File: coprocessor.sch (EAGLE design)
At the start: 51 parts, among them IC1 MEGA32U2, J1 AVR_SPI_PRG_6NS, U1 TPS61090RSAR, U3 V_REG_LDOSMD2, U4 AZV321

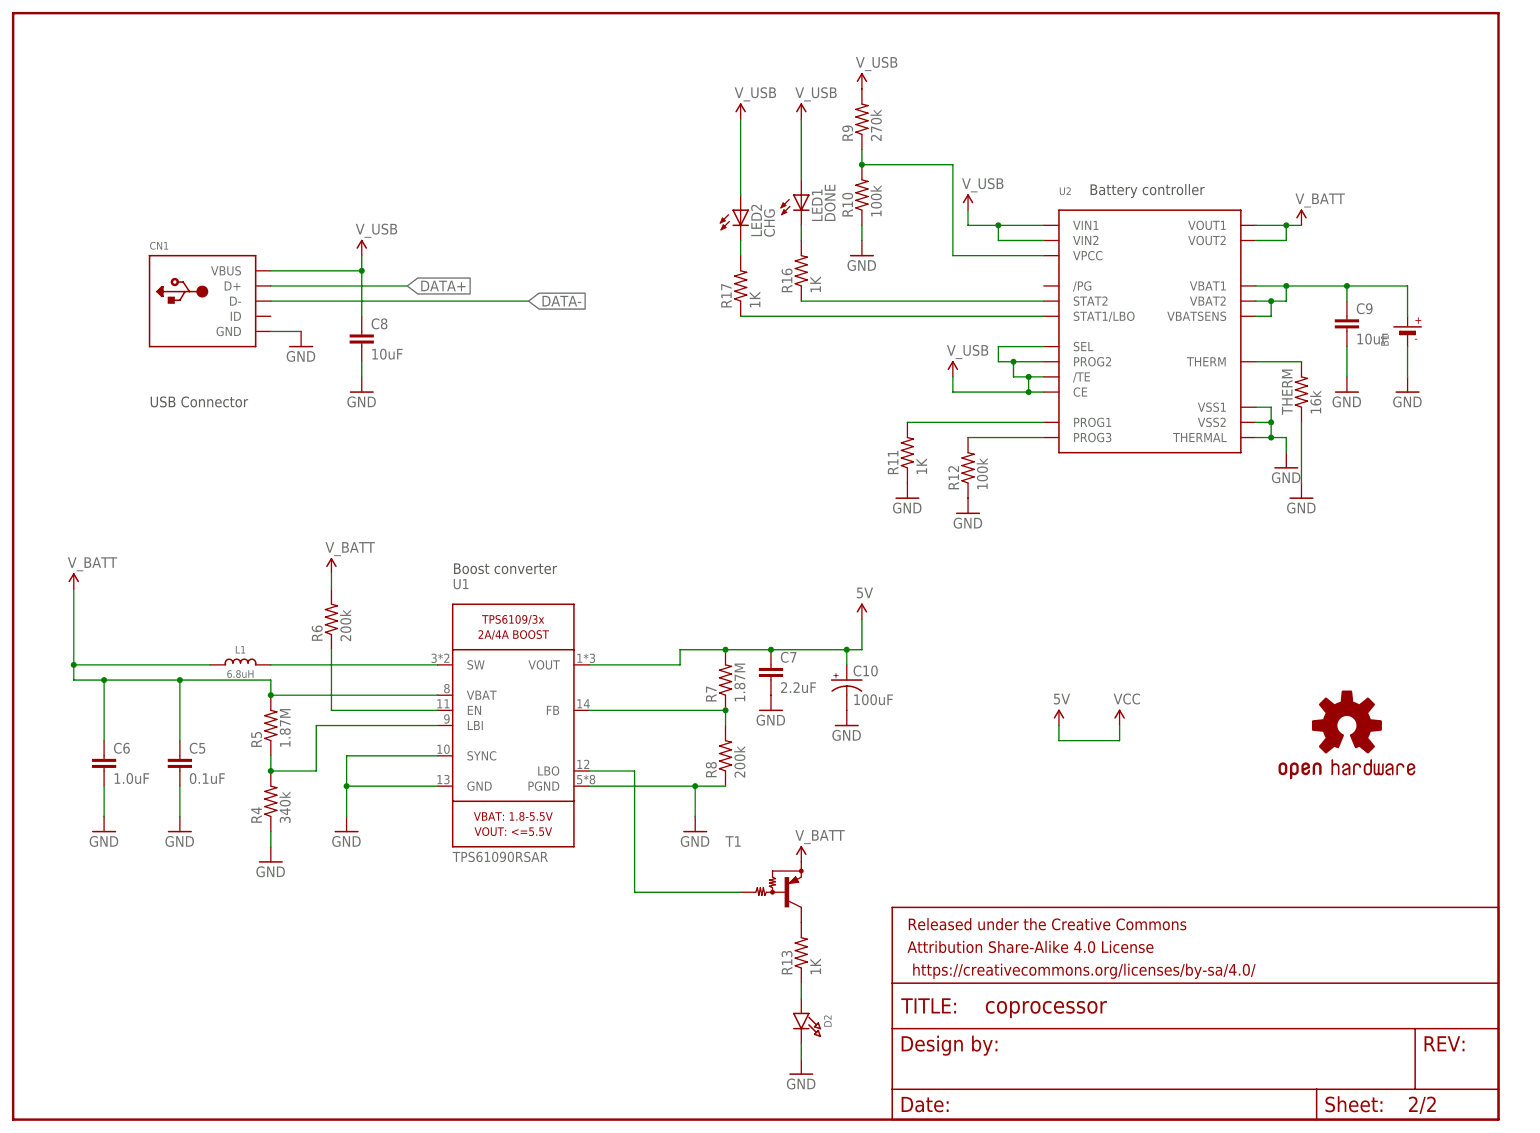
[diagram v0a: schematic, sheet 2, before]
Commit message: final schematic for revision 2
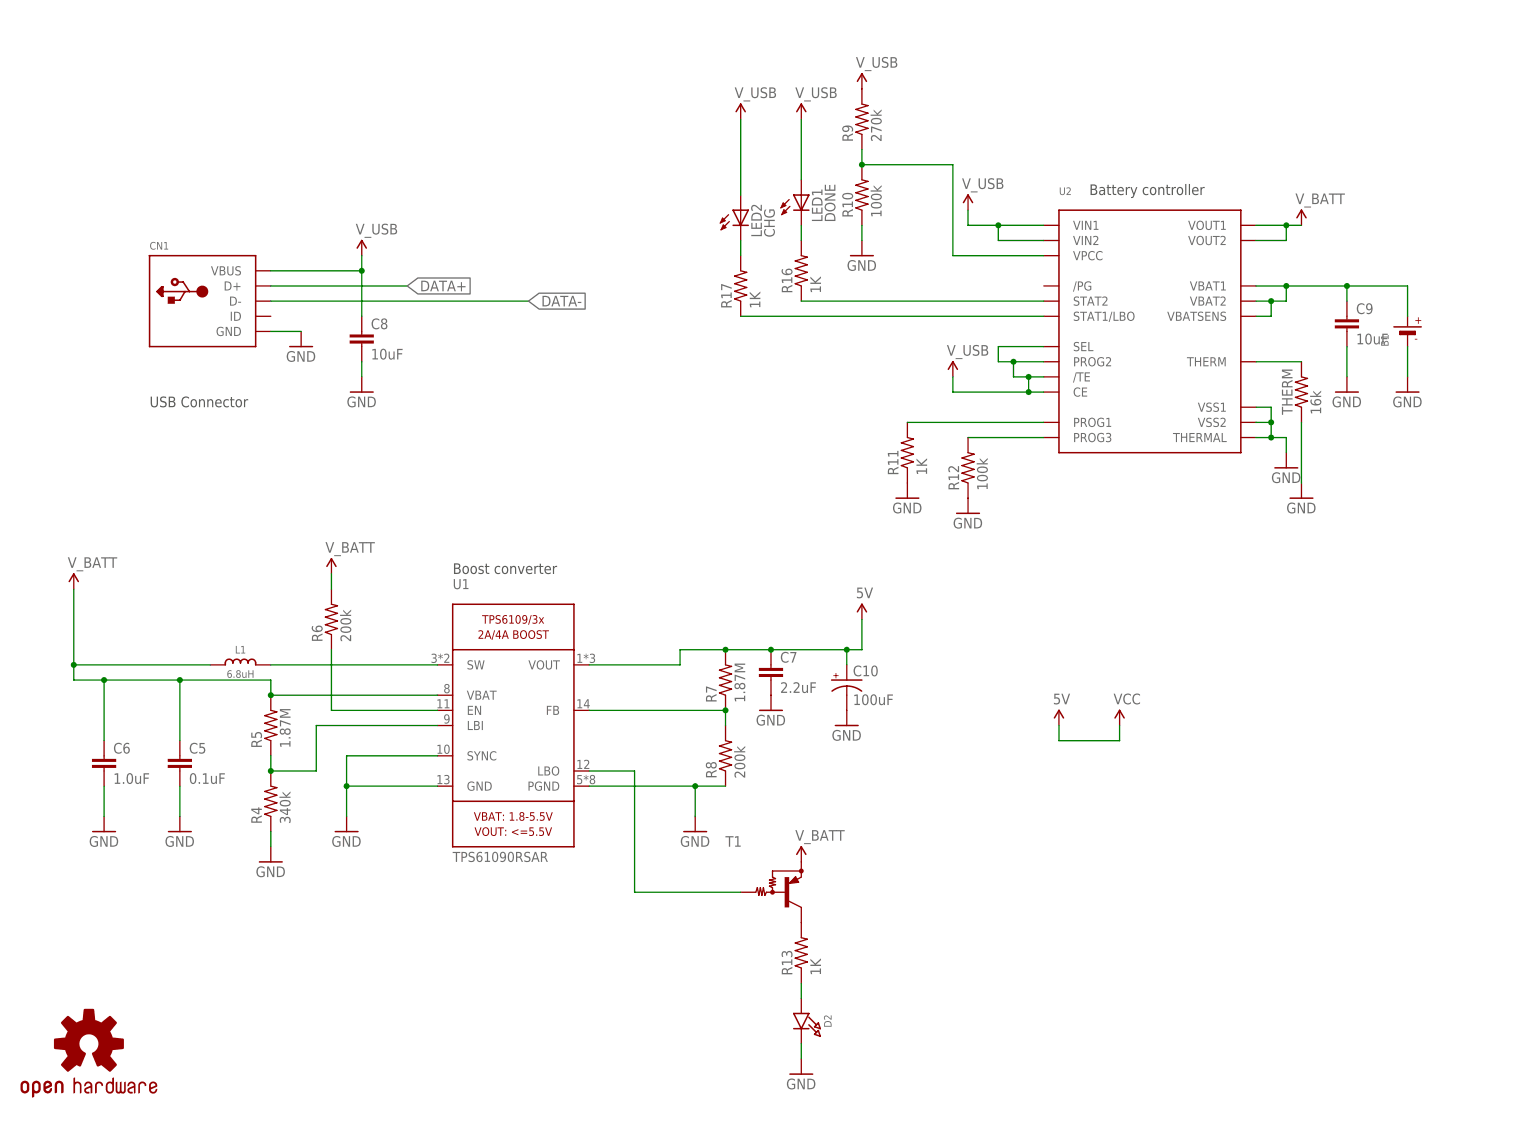
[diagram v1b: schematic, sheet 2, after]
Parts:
- removed FRAME2: Matthew Carlson, SparkFun-Aesthetics:FRAME-LETTER
- removed S1: RESET, SparkFun-Electromechanical:SWITCH-MOMENTARY-2SMD
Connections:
- new net MCU_CS: IC1.PD3(INT3/TXD1), U$3.1A1
- new net MCU_MISO: IC1.PB3(PDO/MISO/PCINT3)
- new net MCU_MOSI: IC1.PB2(PDI/MOSI/PCINT2), U$3.1A3
- new net MCU_RS: IC1.PD2(INT2/AIN1/RXD1), U$3.1A4
- new net MCU_SCK: IC1.PB1(SCK/PCINT1), U$3.1A2
- new net N$28: IC1.PC7(ICP1/INT4/CLKO), J2.5
- new net N$29: IC1.PC6(OC1A/PCINT8), J2.6
- new net N$30: IC1.PC5(OC1B/PCINT9), J2.7
- net GND: now also J2.10; no longer S1.1
- net MISO: no longer IC1.PB3(PDO/MISO/PCINT3)
- net MOSI: no longer IC1.PB2(PDI/MOSI/PCINT2)
- net N$25: now also IC1.PB5(PCINT5), J2.2; no longer U$3.1A2
- net N$26: now also IC1.PB6(PCINT6), J2.3; no longer U$3.1A3
- net N$27: now also IC1.PB7(OC0A/OC1C/PCINT7), J2.4; no longer U$3.1A4
- net N$5: now also IC1.PB4(T1/PCINT4), J2.1; no longer U$3.1A1
- net RESET: now also J2.8; no longer S1.2
- net SCK: no longer IC1.PB1(SCK/PCINT1)
- net TFT_CS: no longer IC1.PD3(INT3/TXD1)
- net TFT_RS: no longer IC1.PD2(INT2/AIN1/RXD1)
- net VCC: now also J2.9
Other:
- moved on the sheet: J2

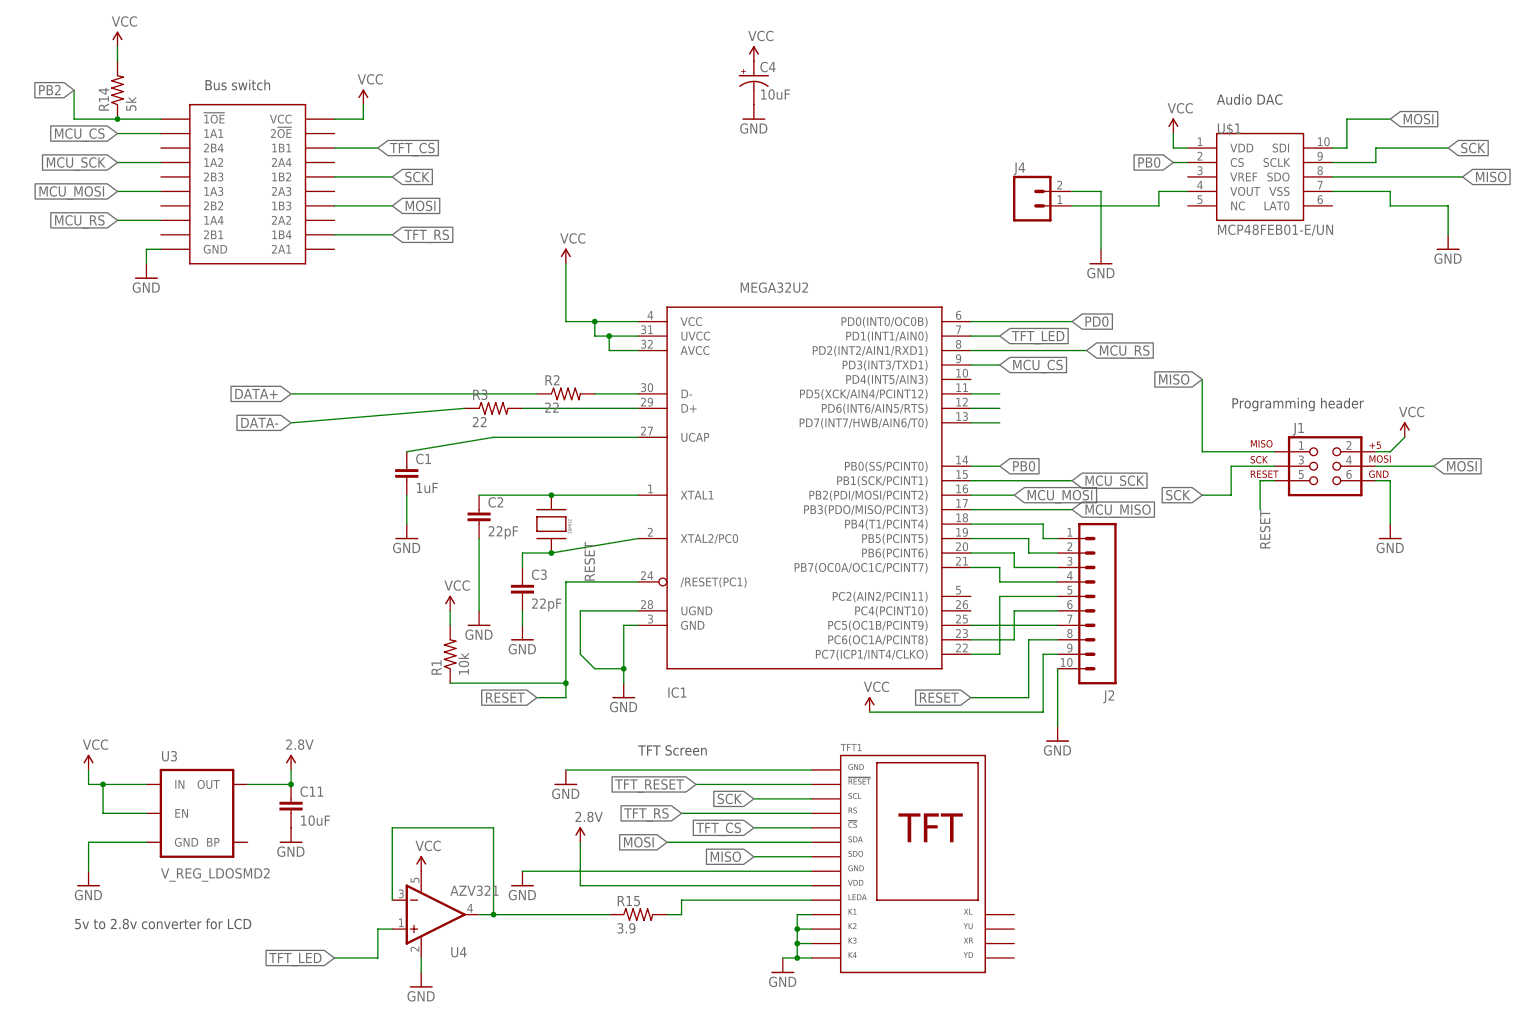
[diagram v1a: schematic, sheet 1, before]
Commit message: fixed a minor bug on the Bus switch PB2->PC2
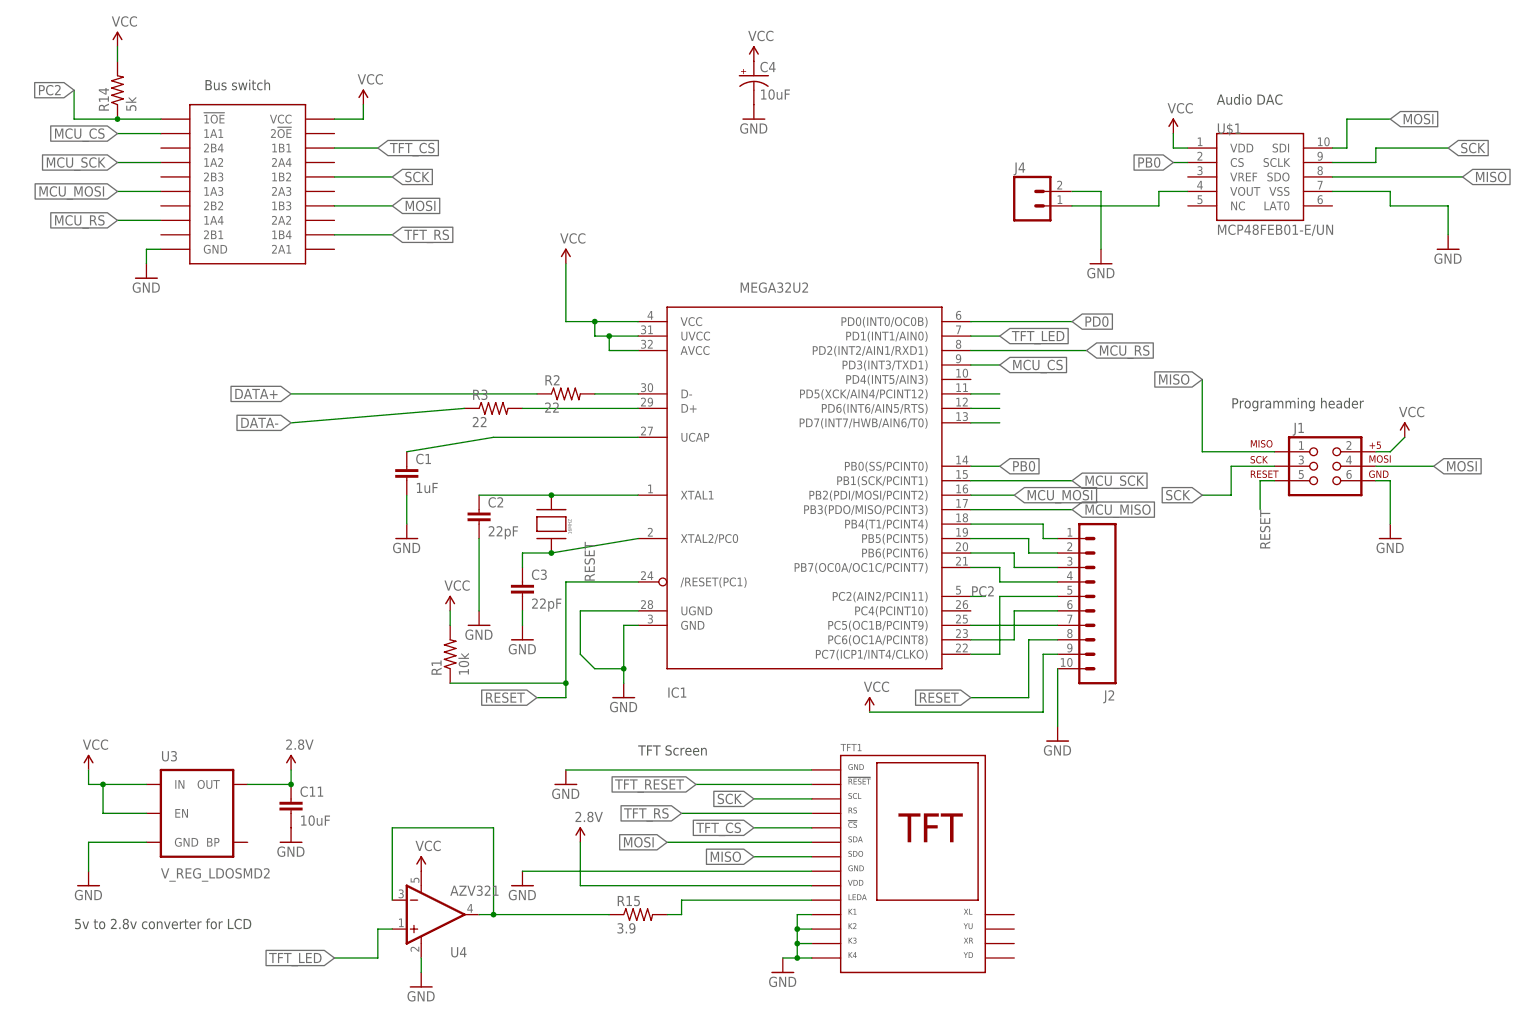
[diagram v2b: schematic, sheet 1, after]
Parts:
- J4: device SparkFun-Connectors:M02POLAR -> SparkFun-Connectors:M02LOCK
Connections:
- removed net PB2: R14.1, U$3.!1OE
- new net PC2: IC1.PC2(AIN2/PCIN11), R14.1, U$3.!1OE
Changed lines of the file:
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@@
 <grid distance="0.1" unitdist="inch" unit="inch" style="lines" multiple="1" display="no" altdistance="0.01" altunitdist="inch" altunit="inch"/>
 <layers>
-<layer number="1" name="Top" color="4" fill="1" visible="no" active="no"/>
-<layer number="2" name="Route2" color="1" fill="3" visible="no" active="no"/>
-<layer number="3" name="Route3" color="4" fill="3" visible="no" active="no"/>
-<layer number="14" name="Route14" color="1" fill="6" visible="no" active="no"/>
-<layer number="15" name="Route15" color="4" fill="6" visible="no" active="no"/>
-<layer number="16" name="Bottom" color="1" fill="1" visible="no" active="no"/>
-<layer number="17" name="Pads" color="2" fill="1" visible="no" active="no"/>
-<layer number="18" name="Vias" color="2" fill="1" visible="no" active="no"/>
-<layer number="19" name="Unrouted" color="6" fill="1" visible="no" active="no"/>
-<layer number="20" name="Dimension" color="15" fill="1" visible="no" active="no"/>
-<layer number="21" name="tPlace" color="7" fill="1" visible="no" active="no"/>
-<layer number="22" name="bPlace" color="7" fill="1" visible="no" active="no"/>
-<layer number="23" name="tOrigins" color="15" fill="1" visible="no" active="no"/>
-<layer number="24" name="bOrigins" color="15" fill="1" visible="no" active="no"/>
-<layer number="25" name="tNames" color="7" fill="1" visible="no" active="no"/>
-<layer number="26" name="bNames" color="7" fill="1" visible="no" active="no"/>
-<layer number="27" name="tValues" color="7" fill="1" visible="no" active="no"/>
-<layer number="28" name="bValues" color="7" fill="1" visible="no" active="no"/>
+<layer number="1" name="Top" color="4" fill="1" visible="yes" active="no"/>
+<layer number="2" name="Route2" color="1" fill="3" visible="yes" active="no"/>
+<layer number="3" name="Route3" color="4" fill="3" visible="yes" active="no"/>
+<layer number="14" name="Route14" color="1" fill="6" visible="yes" active="no"/>
+<layer number="15" name="Route15" color="4" fill="6" visible="yes" active="no"/>
+<layer number="16" name="Bottom" color="1" fill="1" visible="yes" active="no"/>
+<layer number="17" name="Pads" color="2" fill="1" visible="yes" active="no"/>
+<layer number="18" name="Vias" color="2" fill="1" visible="yes" active="no"/>
+<layer number="19" name="Unrouted" color="6" fill="1" visible="yes" active="no"/>
+<layer number="20" name="Dimension" color="15" fill="1" visible="yes" active="no"/>
+<layer number="21" name="tPlace" color="7" fill="1" visible="yes" active="no"/>
+<layer number="22" name="bPlace" color="7" fill="1" visible="yes" active="no"/>
+<layer number="23" name="tOrigins" color="15" fill="1" visible="yes" active="no"/>
+<layer number="24" name="bOrigins" color="15" fill="1" visible="yes" active="no"/>
+<layer number="25" name="tNames" color="7" fill="1" visible="yes" active="no"/>
+<layer number="26" name="bNames" color="7" fill="1" visible="yes" active="no"/>
+<layer number="27" name="tValues" color="7" fill="1" visible="yes" active="no"/>
+<layer number="28" name="bValues" color="7" fill="1" visible="yes" active="no"/>
 <layer number="29" name="tStop" color="7" fill="3" visible="no" active="no"/>
 <layer number="30" name="bStop" color="7" fill="6" visible="no" active="no"/>
@@
 <layer number="35" name="tGlue" color="7" fill="4" visible="no" active="no"/>
 <layer number="36" name="bGlue" color="7" fill="5" visible="no" active="no"/>
-<layer number="37" name="tTest" color="7" fill="1" visible="no" active="no"/>
-<layer number="38" name="bTest" color="7" fill="1" visible="no" active="no"/>
+<layer number="37" name="tTest" color="7" fill="1" visible="yes" active="no"/>
+<layer number="38" name="bTest" color="7" fill="1" visible="yes" active="no"/>
 <layer number="39" name="tKeepout" color="4" fill="11" visible="no" active="no"/>
 <layer number="40" name="bKeepout" color="1" fill="11" visible="no" active="no"/>
@@
 <layer number="44" name="Drills" color="7" fill="1" visible="no" active="no"/>
 <layer number="45" name="Holes" color="7" fill="1" visible="no" active="no"/>
-<layer number="46" name="Milling" color="3" fill="1" visible="no" active="no"/>
-<layer number="47" name="Measures" color="7" fill="1" visible="no" active="no"/>
-<layer number="48" name="Document" color="7" fill="1" visible="no" active="no"/>
-<layer number="49" name="Reference" color="7" fill="1" visible="no" active="no"/>
-<layer number="50" name="dxf" color="7" fill="1" visible="no" active="no"/>
-<layer number="51" name="tDocu" color="7" fill="1" visible="no" active="no"/>
-<layer number="52" name="bDocu" color="7" fill="1" visible="no" active="no"/>
-<layer number="53" name="tGND_GNDA" color="7" fill="9" visible="no" active="no"/>
-<layer number="54" name="bGND_GNDA" color="1" fill="9" visible="no" active="no"/>
-<layer number="56" name="wert" color="7" fill="1" visible="no" active="no"/>
-<layer number="57" name="tCAD" color="7" fill="1" visible="no" active="no"/>
-<layer number="59" name="tCarbon" color="7" fill="1" visible="no" active="no"/>
-<layer number="60" name="bCarbon" color="7" fill="1" visible="no" active="no"/>
+<layer number="46" name="Milling" color="3" fill="1" visible="yes" active="no"/>
+<layer number="47" name="Measures" color="7" fill="1" visible="yes" active="no"/>
+<layer number="48" name="Document" color="7" fill="1" visible="yes" active="no"/>
+<layer number="49" name="Reference" color="7" fill="1" visible="yes" active="no"/>
+<layer number="50" name="dxf" color="7" fill="1" visible="yes" active="no"/>
+<layer number="51" name="tDocu" color="7" fill="1" visible="yes" active="no"/>
+<layer number="52" name="bDocu" color="7" fill="1" visible="yes" active="no"/>
+<layer number="53" name="tGND_GNDA" color="7" fill="9" visible="yes" active="no"/>
+<layer number="54" name="bGND_GNDA" color="1" fill="9" visible="yes" active="no"/>
+<layer number="56" name="wert" color="7" fill="1" visible="yes" active="no"/>
+<layer number="57" name="tCAD" color="7" fill="1" visible="yes" active="no"/>
+<layer number="59" name="tCarbon" color="7" fill="1" visible="yes" active="no"/>
+<layer number="60" name="bCarbon" color="7" fill="1" visible="yes" active="no"/>
 <layer number="90" name="Modules" color="5" fill="1" visible="yes" active="yes"/>
 <layer number="91" name="Nets" color="2" fill="1" visible="yes" active="yes"/>
@@
 <part name="U$1" library="custom" deviceset="MCP48FEB01-E" device="/UN"/>
 <part name="GND9" library="SparkFun-Aesthetics" deviceset="GND" device=""/>
-<part name="J4" library="SparkFun-Connectors" deviceset="M02" device="POLAR"/>
+<part name="J4" library="SparkFun-Connectors" deviceset="M02" device="LOCK"/>
 <part name="GND10" library="SparkFun-Aesthetics" deviceset="GND" device=""/>
 <part name="U$2" library="custom" deviceset="CRYSTAL-ABLS" device="" value="16MHZ"/>
@@
 </segment>
 </net>
-<net name="PB2" class="0">
+<net name="PC2" class="0">
 <segment>
 <pinref part="U$3" gate="G$1" pin="!1OE"/>
@@
 <junction x="-63.5" y="109.22"/>
 </segment>
-</net>
+<segment>
+<pinref part="IC1" gate="G$1" pin="PC2(AIN2/PCIN11)"/>
+<wire x1="86.36" y1="25.4" x2="88.9" y2="25.4" width="0.1524" layer="91"/>
+<label x="86.36" y="25.4" size="1.778" layer="95"/>
+</segment>
+</net>
